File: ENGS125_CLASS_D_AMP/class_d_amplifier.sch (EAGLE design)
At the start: 19 parts, among them M1 ???, M2 ???, U1 LTC6992, U2 LTC4449

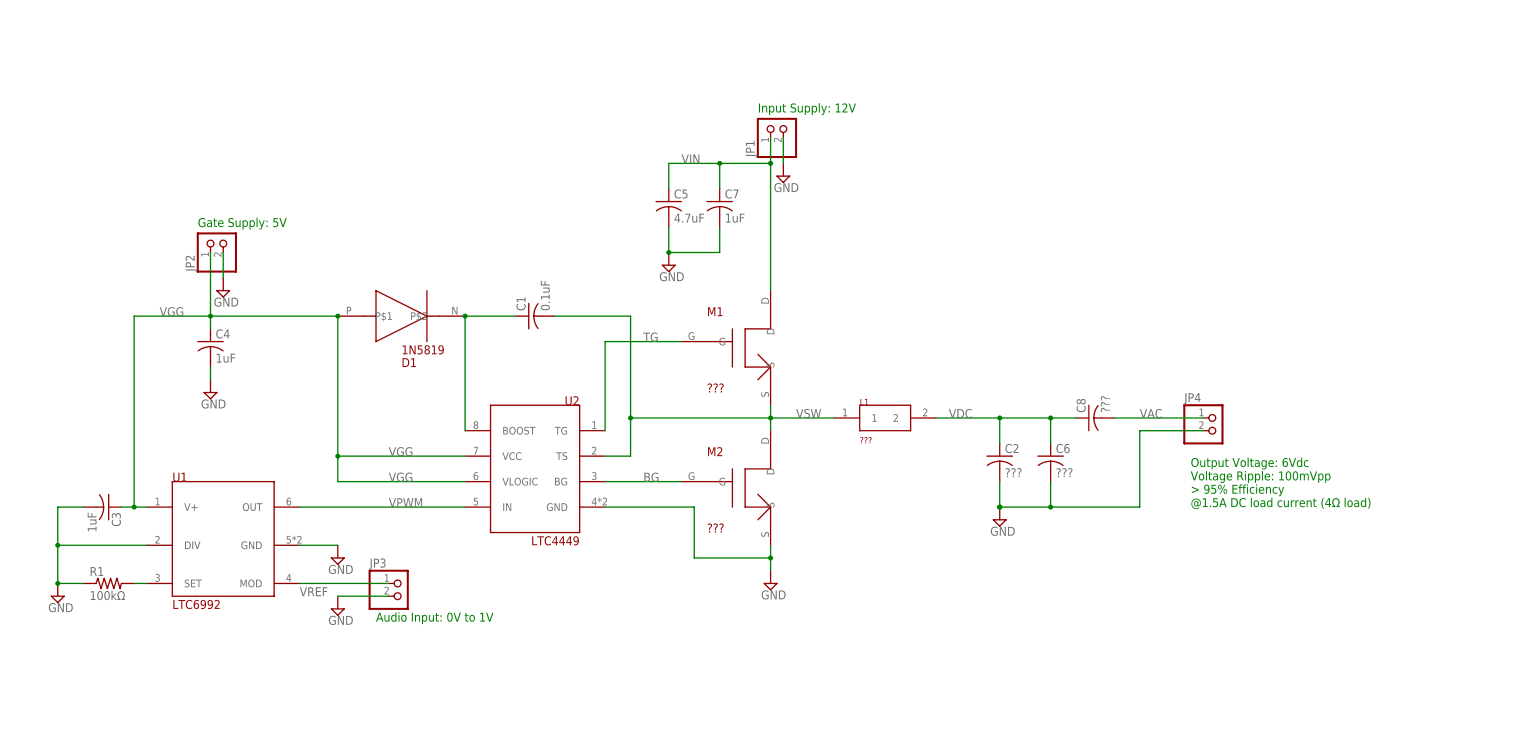
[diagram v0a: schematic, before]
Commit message: Added banana jacks and edited schematic.
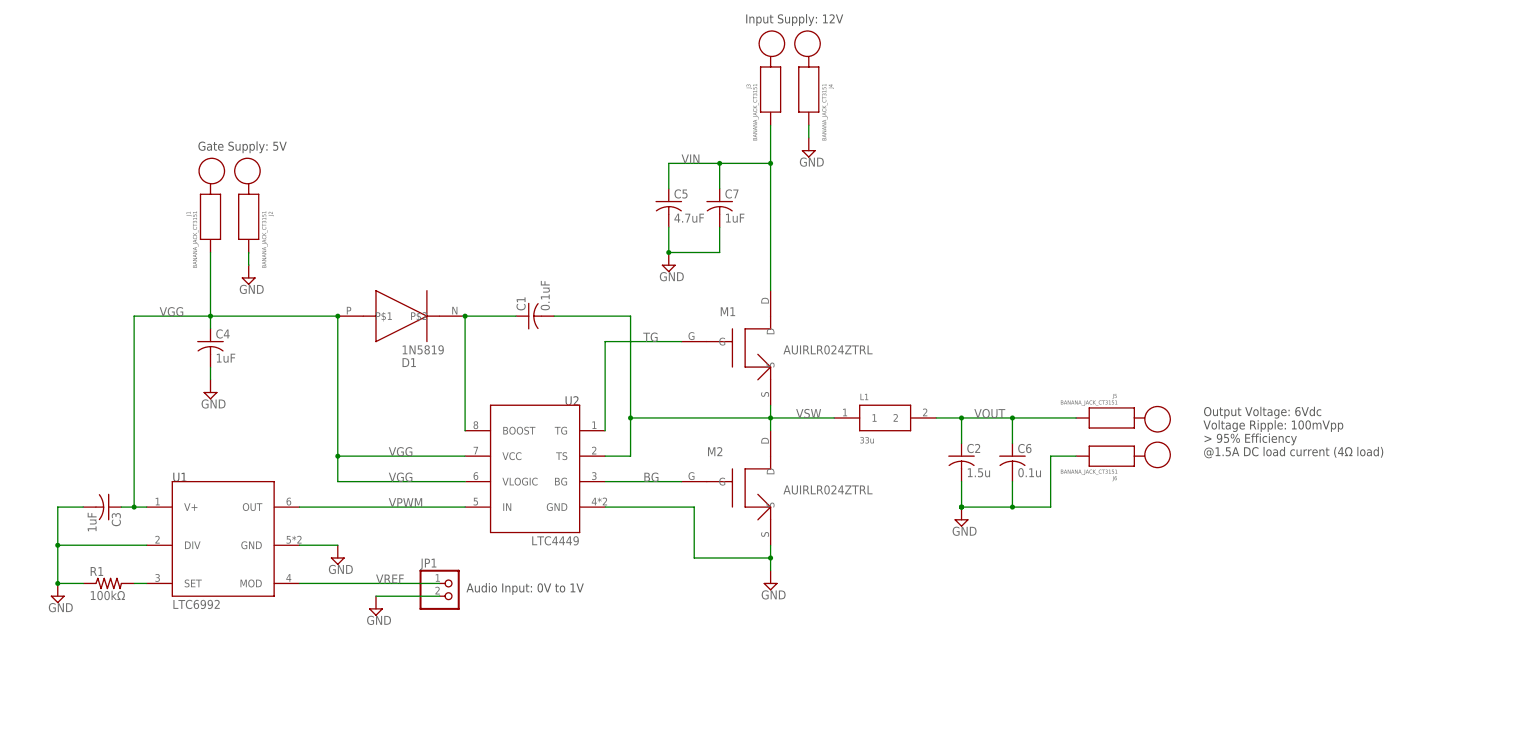
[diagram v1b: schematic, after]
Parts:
- removed C8: ???, Engs125_library:C-US
- removed JP2, JP3, JP4: (no value), Engs125_library:PINHD-1X2
- added J1, J2, J3, J4, J5, J6: BANANA_JACK_CT3151, Engs125_lib_UPDATEFeb22:BANANA_JACK_CT3151
- C2: value ??? -> 1.5u
- C6: value ??? -> 0.1u
- JP1: device Engs125_library:PINHD-1X2 -> Engs125_lib_UPDATEFeb22:PINHD-1X2
- L1: value ??? -> 33u
- M1, M2: value ??? -> AUIRLR024ZTRL
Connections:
- removed net VAC: C8.2, JP4.1
- removed net VDC: C2.1, C6.1, C8.1, L1.2
- new net VOUT: C2.1, C6.1, J5.IN, L1.2
- net GND: now also J2.IN, J4.IN, J6.IN; no longer JP2.2, JP3.2, JP4.2
- net VGG: now also J1.IN; no longer JP2.1
- net VIN: now also J3.IN; no longer JP1.1
- net VREF: now also JP1.1; no longer JP3.1
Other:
- moved on the sheet: C2, C6, JP1

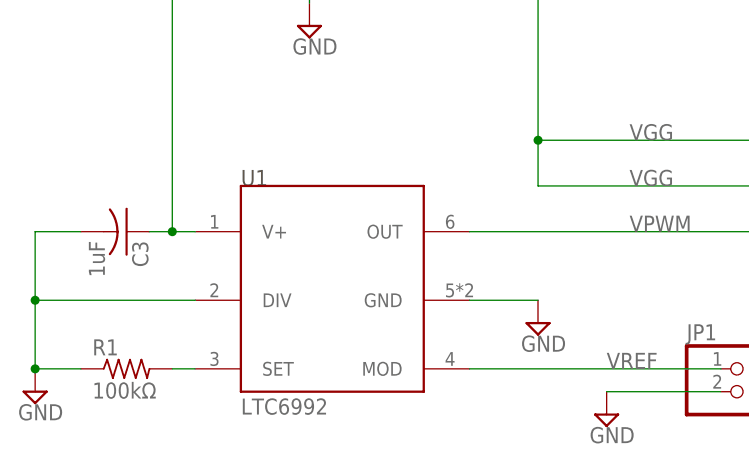
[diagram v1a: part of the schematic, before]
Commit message: Updated package for LTC6992 (PWM modulator)
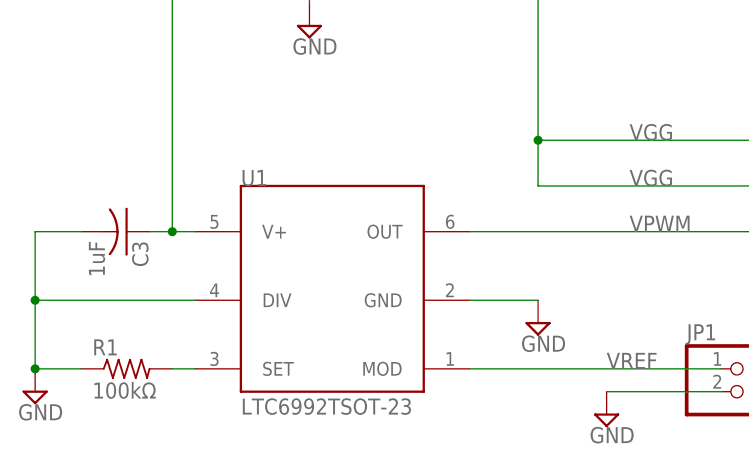
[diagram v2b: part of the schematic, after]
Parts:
- U1: value LTC6992 -> LTC6992TSOT-23; device Engs125_library:LTC6992 -> Engs125_lib_UPDATEFeb22:LTC6992TSOT-23
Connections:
- new net N$3: U1.GND
- net GND: no longer U1.GND
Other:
- moved on the sheet: U1
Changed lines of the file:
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@@
 <parts>
 <part name="U2" library="Engs125_library" deviceset="LTC4449" device=""/>
-<part name="U1" library="Engs125_library" deviceset="LTC6992" device=""/>
 <part name="SUPPLY1" library="Engs125_library" deviceset="GND" device=""/>
 <part name="C3" library="Engs125_library" deviceset="C-US" device="" value="1uF"/>
@@
 <part name="J5" library="Engs125_lib_UPDATEFeb22" deviceset="BANANA_JACK_CT3151" device=""/>
 <part name="J6" library="Engs125_lib_UPDATEFeb22" deviceset="BANANA_JACK_CT3151" device=""/>
+<part name="U1" library="Engs125_lib_UPDATEFeb22" deviceset="LTC6992" device="TSOT-23"/>
 </parts>
 <sheets>
@@
 <attribute name="VALUE" x="91.44" y="53.34" size="1.778" layer="96" rot="MR0"/>
 </instance>
-<instance part="U1" gate="G$1" x="20.32" y="53.34" smashed="yes">
-<attribute name="NAME" x="10.16" y="66.04" size="1.778" layer="97"/>
-<attribute name="VALUE" x="10.16" y="40.64" size="1.778" layer="96"/>
-</instance>
 <instance part="SUPPLY1" gate="GND" x="-12.7" y="43.18" smashed="yes">
 <attribute name="VALUE" x="-14.605" y="40.005" size="1.778" layer="96"/>
@@
 <attribute name="VALUE" x="198.82" y="67.62" size="0.8128" layer="96" rot="MR0"/>
 <attribute name="NAME" x="198.72" y="66.32" size="0.8128" layer="95" rot="MR0"/>
+</instance>
+<instance part="U1" gate="G$1" x="20.32" y="53.34" smashed="yes">
+<attribute name="NAME" x="10.16" y="66.04" size="1.778" layer="95"/>
+<attribute name="VALUE" x="10.16" y="40.64" size="1.778" layer="96"/>
 </instance>
 </instances>
@@
 <net name="N$1" class="0">
 <segment>
-<pinref part="U1" gate="G$1" pin="SET"/>
 <pinref part="R1" gate="G$1" pin="2"/>
 <wire x1="5.08" y1="45.72" x2="2.54" y2="45.72" width="0.1524" layer="91"/>
+<pinref part="U1" gate="G$1" pin="SET"/>
 </segment>
 </net>
@@
 <pinref part="SUPPLY1" gate="GND" pin="GND"/>
 <wire x1="-7.62" y1="45.72" x2="-12.7" y2="45.72" width="0.1524" layer="91"/>
-<pinref part="U1" gate="G$1" pin="DIV"/>
 <wire x1="5.08" y1="53.34" x2="-12.7" y2="53.34" width="0.1524" layer="91"/>
 <wire x1="-12.7" y1="53.34" x2="-12.7" y2="45.72" width="0.1524" layer="91"/>
@@
 <wire x1="-12.7" y1="60.96" x2="-12.7" y2="53.34" width="0.1524" layer="91"/>
 <junction x="-12.7" y="53.34"/>
+<pinref part="U1" gate="G$1" pin="DIV"/>
 </segment>
 <segment>
@@
 </segment>
 <segment>
-<pinref part="SUPPLY2" gate="GND" pin="GND"/>
-<pinref part="U1" gate="G$1" pin="GND"/>
-<wire x1="43.18" y1="53.34" x2="35.56" y2="53.34" width="0.1524" layer="91"/>
-</segment>
-<segment>
 <pinref part="SUPPLY3" gate="GND" pin="GND"/>
 <wire x1="50.8" y1="43.18" x2="63.5" y2="43.18" width="0.1524" layer="91"/>
@@
 <net name="VGG" class="0">
 <segment>
-<pinref part="U1" gate="G$1" pin="V+"/>
 <pinref part="C3" gate="G$1" pin="1"/>
 <wire x1="5.08" y1="60.96" x2="2.54" y2="60.96" width="0.1524" layer="91"/>
@@
 <label x="53.34" y="66.04" size="1.778" layer="95"/>
 <pinref part="J1" gate="G$1" pin="IN"/>
+<pinref part="U1" gate="G$1" pin="V+"/>
 </segment>
 </net>
 <net name="VPWM" class="0">
 <segment>
-<pinref part="U1" gate="G$1" pin="OUT"/>
 <pinref part="U2" gate="G$1" pin="IN"/>
 <wire x1="35.56" y1="60.96" x2="68.58" y2="60.96" width="0.1524" layer="91"/>
 <label x="53.34" y="60.96" size="1.778" layer="95"/>
+<pinref part="U1" gate="G$1" pin="OUT"/>
 </segment>
 </net>
@@
 <net name="VREF" class="0">
 <segment>
-<pinref part="U1" gate="G$1" pin="MOD"/>
 <wire x1="35.56" y1="45.72" x2="63.5" y2="45.72" width="0.1524" layer="91"/>
 <label x="50.8" y="45.72" size="1.778" layer="95"/>
 <pinref part="JP1" gate="G$1" pin="1"/>
-</segment>
-</net>
+<pinref part="U1" gate="G$1" pin="MOD"/>
+</segment>
+</net>
+<net name="N$3" class="0">
+<segment>
+<pinref part="SUPPLY2" gate="GND" pin="GND"/>
+<wire x1="43.18" y1="53.34" x2="35.56" y2="53.34" width="0.1524" layer="91"/>
+<pinref part="U1" gate="G$1" pin="GND"/>
+</segment>
+</net>

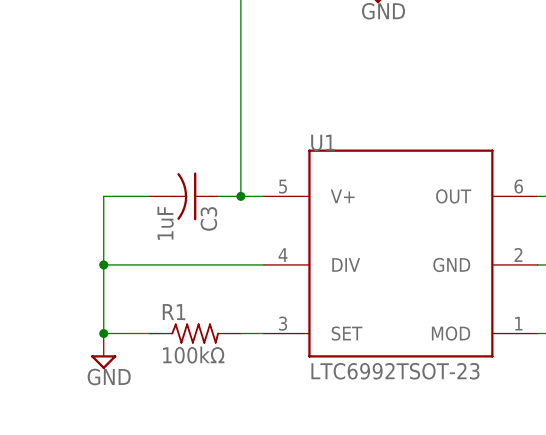
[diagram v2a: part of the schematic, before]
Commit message: Replaced Rset with trim potentiometer
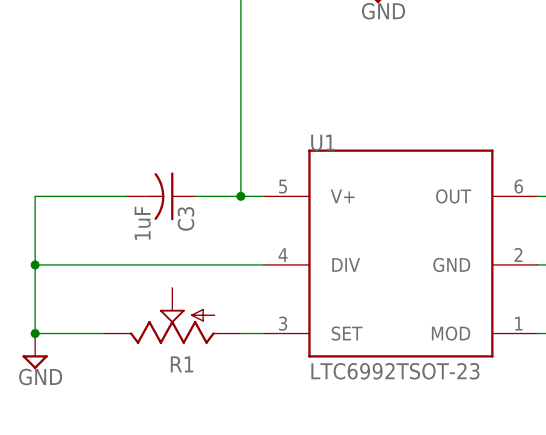
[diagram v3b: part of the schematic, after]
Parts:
- R1: value 100kΩ -> (none); device Engs125_library:R-US -> Engs125_lib_UPDATEFeb22:TRIM_US-CT6
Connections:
- net GND: now also R1.E; no longer R1.1
- net N$1: now also R1.A; no longer R1.2
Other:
- moved on the sheet: C3
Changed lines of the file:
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@@
 <part name="M1" library="Engs125_library" deviceset="MOSFET_DPAK" device="" value="AUIRLR024ZTRL"/>
 <part name="M2" library="Engs125_library" deviceset="MOSFET_DPAK" device="" value="AUIRLR024ZTRL"/>
-<part name="R1" library="Engs125_library" deviceset="R-US" device="" value="100kΩ"/>
 <part name="L1" library="Engs125_library" deviceset="SER2900" device="SER" value="33u"/>
 <part name="SUPPLY2" library="Engs125_library" deviceset="GND" device=""/>
@@
 <part name="J6" library="Engs125_lib_UPDATEFeb22" deviceset="BANANA_JACK_CT3151" device=""/>
 <part name="U1" library="Engs125_lib_UPDATEFeb22" deviceset="LTC6992" device="TSOT-23"/>
+<part name="R1" library="Engs125_lib_UPDATEFeb22" deviceset="TRIM_US-" device="CT6"/>
 </parts>
 <sheets>
@@
 <attribute name="VALUE" x="91.44" y="53.34" size="1.778" layer="96" rot="MR0"/>
 </instance>
-<instance part="SUPPLY1" gate="GND" x="-12.7" y="43.18" smashed="yes">
-<attribute name="VALUE" x="-14.605" y="40.005" size="1.778" layer="96"/>
-</instance>
-<instance part="C3" gate="G$1" x="-2.54" y="60.96" smashed="yes" rot="R270">
-<attribute name="NAME" x="-1.905" y="59.944" size="1.778" layer="95" rot="R270"/>
-<attribute name="VALUE" x="-6.731" y="59.944" size="1.778" layer="96" rot="R270"/>
+<instance part="SUPPLY1" gate="GND" x="-20.32" y="43.18" smashed="yes">
+<attribute name="VALUE" x="-22.225" y="40.005" size="1.778" layer="96"/>
+</instance>
+<instance part="C3" gate="G$1" x="-5.08" y="60.96" smashed="yes" rot="R270">
+<attribute name="NAME" x="-4.445" y="59.944" size="1.778" layer="95" rot="R270"/>
+<attribute name="VALUE" x="-9.271" y="59.944" size="1.778" layer="96" rot="R270"/>
 </instance>
 <instance part="C4" gate="G$1" x="17.78" y="93.98" smashed="yes">
@@
 <attribute name="VALUE" x="132.08" y="63.5" size="1.778" layer="96"/>
 </instance>
-<instance part="R1" gate="G$1" x="-2.54" y="45.72" smashed="yes">
-<attribute name="NAME" x="-6.35" y="47.2186" size="1.778" layer="95"/>
-<attribute name="VALUE" x="-6.35" y="42.418" size="1.778" layer="96"/>
-</instance>
 <instance part="L1" gate="G$1" x="152.4" y="78.74" smashed="yes">
 <attribute name="VALUE" x="147.32" y="73.66" size="1.27" layer="96"/>
@@
 <attribute name="NAME" x="10.16" y="66.04" size="1.778" layer="95"/>
 <attribute name="VALUE" x="10.16" y="40.64" size="1.778" layer="96"/>
+</instance>
+<instance part="R1" gate="G$1" x="-5.08" y="45.72" smashed="yes" rot="R90">
+<attribute name="NAME" x="-2.54" y="43.18" size="1.778" layer="95" rot="R180"/>
+<attribute name="VALUE" x="-2.54" y="43.18" size="1.778" layer="96" rot="R180"/>
 </instance>
 </instances>
@@
 <net name="N$1" class="0">
 <segment>
-<pinref part="R1" gate="G$1" pin="2"/>
 <wire x1="5.08" y1="45.72" x2="2.54" y2="45.72" width="0.1524" layer="91"/>
 <pinref part="U1" gate="G$1" pin="SET"/>
+<pinref part="R1" gate="G$1" pin="A"/>
 </segment>
 </net>
 <net name="GND" class="0">
 <segment>
-<pinref part="R1" gate="G$1" pin="1"/>
 <pinref part="SUPPLY1" gate="GND" pin="GND"/>
-<wire x1="-7.62" y1="45.72" x2="-12.7" y2="45.72" width="0.1524" layer="91"/>
-<wire x1="5.08" y1="53.34" x2="-12.7" y2="53.34" width="0.1524" layer="91"/>
-<wire x1="-12.7" y1="53.34" x2="-12.7" y2="45.72" width="0.1524" layer="91"/>
-<junction x="-12.7" y="45.72"/>
+<wire x1="-12.7" y1="45.72" x2="-20.32" y2="45.72" width="0.1524" layer="91"/>
+<wire x1="5.08" y1="53.34" x2="-20.32" y2="53.34" width="0.1524" layer="91"/>
+<wire x1="-20.32" y1="53.34" x2="-20.32" y2="45.72" width="0.1524" layer="91"/>
+<junction x="-20.32" y="45.72"/>
 <pinref part="C3" gate="G$1" pin="2"/>
-<wire x1="-7.62" y1="60.96" x2="-12.7" y2="60.96" width="0.1524" layer="91"/>
-<wire x1="-12.7" y1="60.96" x2="-12.7" y2="53.34" width="0.1524" layer="91"/>
-<junction x="-12.7" y="53.34"/>
+<wire x1="-10.16" y1="60.96" x2="-20.32" y2="60.96" width="0.1524" layer="91"/>
+<wire x1="-20.32" y1="60.96" x2="-20.32" y2="53.34" width="0.1524" layer="91"/>
+<junction x="-20.32" y="53.34"/>
 <pinref part="U1" gate="G$1" pin="DIV"/>
+<pinref part="R1" gate="G$1" pin="E"/>
 </segment>
 <segment>
@@
 <pinref part="C3" gate="G$1" pin="1"/>
 <wire x1="5.08" y1="60.96" x2="2.54" y2="60.96" width="0.1524" layer="91"/>
-<wire x1="2.54" y1="60.96" x2="0" y2="60.96" width="0.1524" layer="91"/>
+<wire x1="2.54" y1="60.96" x2="-2.54" y2="60.96" width="0.1524" layer="91"/>
 <wire x1="2.54" y1="60.96" x2="2.54" y2="99.06" width="0.1524" layer="91"/>
 <wire x1="2.54" y1="99.06" x2="17.78" y2="99.06" width="0.1524" layer="91"/>
